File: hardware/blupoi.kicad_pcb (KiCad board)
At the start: 2 copper layers, 505.1 x 22.2 mm, 208 parts, among them P1 MICRO-B-USB, SW1 PM_BTN, U1 NRF52832, U2 TPS63031DSKR, U3 bno055, U4 ics43432, U5 BQ24075RGTT, U6 MAX16054AZT+T, X1 32MHz

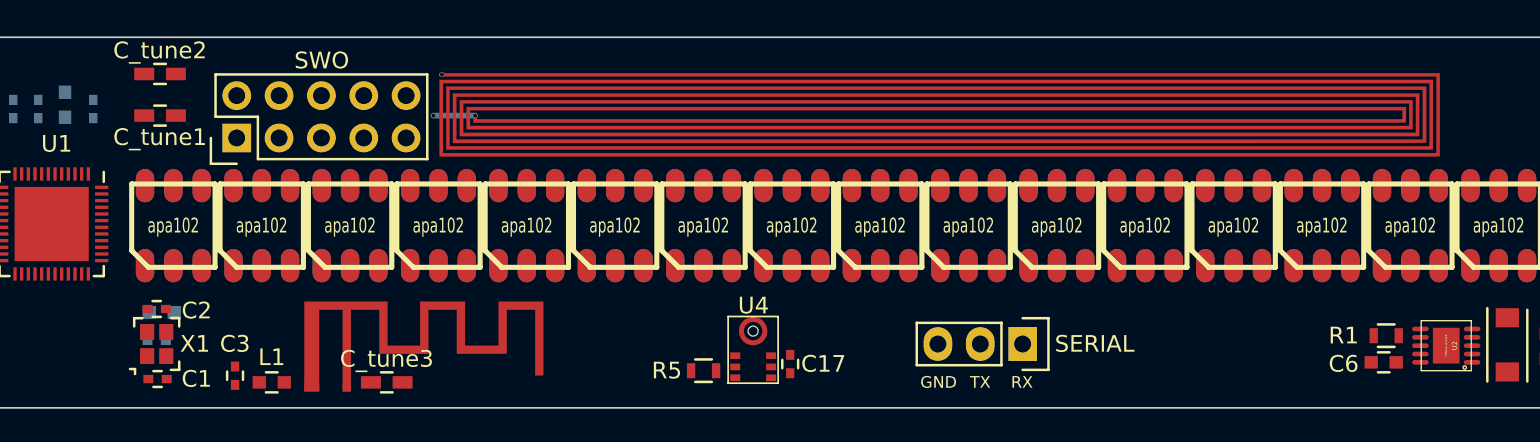
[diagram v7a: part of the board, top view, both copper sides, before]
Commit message: Increased MIC pad sizes
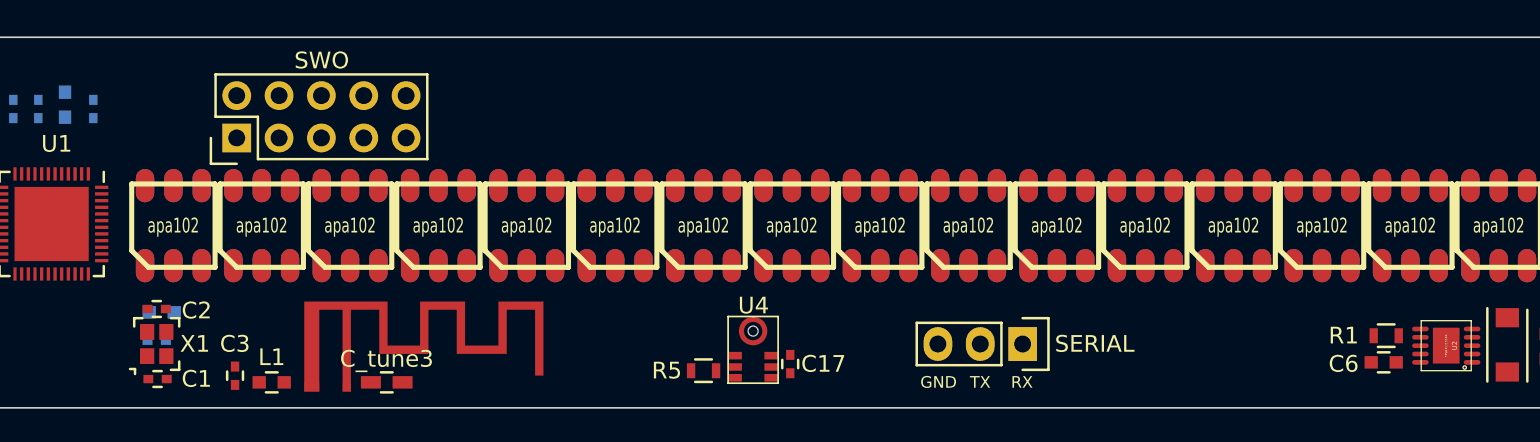
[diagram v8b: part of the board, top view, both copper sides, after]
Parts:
- removed ANT2: ANT_NFC, nfc_antenna:nfc_antenna_60x5mm_1.826uH
- removed C_tune1, C_tune2: TDB, Capacitors_SMD:C_0603_HandSoldering
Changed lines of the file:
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@@
 (kicad_pcb (version 20170123) (host pcbnew no-vcs-found-7591~57~ubuntu16.10.1)
   (general
-    (links 799)
-    (no_connects 783)
+    (links 793)
+    (no_connects 777)
     (area -67.365001 99.149999 437.850001 121.480001)
     (thickness 1.6)
@@
     (tracks 0)
     (zones 0)
-    (modules 208)
+    (modules 205)
     (nets 345)
   )
@@
     (pad 4 smd circle (at 1.1565 1.5 90) (size 1.65 1.65) (layers F.Paste F.Mask)
       (net 2 GND))
-    (pad 7 smd rect (at -1.6435 0.425 90) (size 0.4 0.6) (layers F.Cu F.Paste F.Mask)
+    (pad 7 smd rect (at -1.6435 0.425 90) (size 0.45 0.8) (layers F.Cu F.Paste F.Mask)
       (net 322 MIC_I2S_SD))
-    (pad 6 smd rect (at -0.9935 0.425 90) (size 0.4 0.6) (layers F.Cu F.Paste F.Mask)
+    (pad 6 smd rect (at -0.9935 0.425 90) (size 0.45 0.8) (layers F.Cu F.Paste F.Mask)
       (net 324 MIC_I2S_SCK))
-    (pad 5 smd rect (at -0.3185 0.425 90) (size 0.4 0.6) (layers F.Cu F.Paste F.Mask)
+    (pad 5 smd rect (at -0.3185 0.425 90) (size 0.45 0.8) (layers F.Cu F.Paste F.Mask)
       (net 325 MIC_I2S_WS))
-    (pad 3 smd rect (at -0.3185 2.575 90) (size 0.4 0.6) (layers F.Cu F.Paste F.Mask)
+    (pad 3 smd rect (at -0.3185 2.575 90) (size 0.45 0.8) (layers F.Cu F.Paste F.Mask)
       (net 328 V3.3))
-    (pad 2 smd rect (at -0.9935 2.575 90) (size 0.4 0.6) (layers F.Cu F.Paste F.Mask)
+    (pad 2 smd rect (at -0.9935 2.575 90) (size 0.45 0.8) (layers F.Cu F.Paste F.Mask)
       (net 2 GND))
-    (pad 1 smd rect (at -1.6435 2.575 90) (size 0.4 0.6) (layers F.Cu F.Paste F.Mask)
+    (pad 1 smd rect (at -1.6435 2.575 90) (size 0.45 0.8) (layers F.Cu F.Paste F.Mask)
       (net 328 V3.3))
   )
@@
   )
   (module Capacitors_SMD:C_0603_HandSoldering (layer F.Cu)
-    (at -44.5 103.9)
-    (descr "Capacitor SMD 0603, hand soldering")
-    (tags "capacitor 0603")
-    (attr smd)
-    (fp_text reference C_tune1 (at 0 1.3 -180) (layer F.SilkS)
-      (effects (font (size 1 1) (thickness 0.15)))
-    )
-    (fp_text value TDB (at 0 1.9) (layer F.Fab)
-      (effects (font (size 1 1) (thickness 0.15)))
-    )
-    (fp_line (start -1.85 -0.75) (end 1.85 -0.75) (layer F.CrtYd) (width 0.05))
-    (fp_line (start -1.85 0.75) (end 1.85 0.75) (layer F.CrtYd) (width 0.05))
-    (fp_line (start -1.85 -0.75) (end -1.85 0.75) (layer F.CrtYd) (width 0.05))
-    (fp_line (start 1.85 -0.75) (end 1.85 0.75) (layer F.CrtYd) (width 0.05))
-    (fp_line (start -0.35 -0.6) (end 0.35 -0.6) (layer F.SilkS) (width 0.15))
-    (fp_line (start 0.35 0.6) (end -0.35 0.6) (layer F.SilkS) (width 0.15))
-    (pad 1 smd rect (at -0.95 0) (size 1.2 0.75) (layers F.Cu F.Paste F.Mask)
-      (net 2 GND))
-    (pad 2 smd rect (at 0.95 0) (size 1.2 0.75) (layers F.Cu F.Paste F.Mask)
-      (net 133 "Net-(ANT2-Pad1)"))
-    (model Capacitors_SMD.3dshapes/C_0603_HandSoldering.wrl
-      (at (xyz 0 0 0))
-      (scale (xyz 1 1 1))
-      (rotate (xyz 0 0 0))
-    )
-  )
-  (module Capacitors_SMD:C_0603_HandSoldering (layer F.Cu)
-    (at -44.5 101.4 180)
-    (descr "Capacitor SMD 0603, hand soldering")
-    (tags "capacitor 0603")
-    (attr smd)
-    (fp_text reference C_tune2 (at 0 1.4) (layer F.SilkS)
-      (effects (font (size 1 1) (thickness 0.15)))
-    )
-    (fp_text value TDB (at 0 1.9 180) (layer F.Fab)
-      (effects (font (size 1 1) (thickness 0.15)))
-    )
-    (fp_line (start -1.85 -0.75) (end 1.85 -0.75) (layer F.CrtYd) (width 0.05))
-    (fp_line (start -1.85 0.75) (end 1.85 0.75) (layer F.CrtYd) (width 0.05))
-    (fp_line (start -1.85 -0.75) (end -1.85 0.75) (layer F.CrtYd) (width 0.05))
-    (fp_line (start 1.85 -0.75) (end 1.85 0.75) (layer F.CrtYd) (width 0.05))
-    (fp_line (start -0.35 -0.6) (end 0.35 -0.6) (layer F.SilkS) (width 0.15))
-    (fp_line (start 0.35 0.6) (end -0.35 0.6) (layer F.SilkS) (width 0.15))
-    (pad 1 smd rect (at -0.95 0 180) (size 1.2 0.75) (layers F.Cu F.Paste F.Mask)
-      (net 139 "Net-(ANT2-Pad2)"))
-    (pad 2 smd rect (at 0.95 0 180) (size 1.2 0.75) (layers F.Cu F.Paste F.Mask)
-      (net 2 GND))
-    (model Capacitors_SMD.3dshapes/C_0603_HandSoldering.wrl
-      (at (xyz 0 0 0))
-      (scale (xyz 1 1 1))
-      (rotate (xyz 0 0 0))
-    )
-  )
-  (module Capacitors_SMD:C_0603_HandSoldering (layer F.Cu)
     (at -30.9 119.9)
     (descr "Capacitor SMD 0603, hand soldering")
@@
     )
   )
-  (module nfc_antenna:nfc_antenna_60x5mm_1.826uH (layer F.Cu)
-    (at 2.255 103.85)
-    (fp_text reference ANT2 (at 0.0635 -5.08) (layer F.SilkS) hide
-      (effects (font (thickness 0.3)))
-    )
-    (fp_text value ANT_NFC (at 0 -3.429) (layer F.SilkS) hide
-      (effects (font (thickness 0.3)))
-    )
-    (fp_line (start -27.8765 0.05) (end -30.353 0.05) (layer B.Cu) (width 0.35))
-    (fp_poly (pts (xy 30.011709 0.002646) (xy 30.009042 2.502958) (xy 0.007937 2.505606) (xy -29.993167 2.508254)
-      (xy -29.993167 -2.0955) (xy 29.601636 -2.0955) (xy 29.596292 2.090208) (xy -29.591 2.095504)
-      (xy -29.591 -1.693333) (xy 29.199417 -1.693333) (xy 29.199416 -0.015119) (xy 29.199396 0.208707)
-      (xy 29.19933 0.412297) (xy 29.199209 0.596581) (xy 29.199026 0.762489) (xy 29.198771 0.910953)
-      (xy 29.198437 1.042903) (xy 29.198016 1.159269) (xy 29.197498 1.260981) (xy 29.196877 1.34897)
-      (xy 29.196142 1.424167) (xy 29.195287 1.487501) (xy 29.194303 1.539904) (xy 29.193181 1.582306)
-      (xy 29.191914 1.615637) (xy 29.190492 1.640827) (xy 29.188908 1.658808) (xy 29.187153 1.670509)
-      (xy 29.18522 1.676861) (xy 29.184297 1.678214) (xy 29.181827 1.678713) (xy 29.175277 1.679202)
-      (xy 29.164426 1.67968) (xy 29.14905 1.680147) (xy 29.128928 1.680603) (xy 29.103837 1.68105)
-      (xy 29.073554 1.681486) (xy 29.037858 1.681911) (xy 28.996525 1.682327) (xy 28.949333 1.682733)
-      (xy 28.896061 1.683129) (xy 28.836485 1.683515) (xy 28.770383 1.683892) (xy 28.697533 1.684259)
-      (xy 28.617712 1.684617) (xy 28.530697 1.684966) (xy 28.436268 1.685305) (xy 28.3342 1.685636)
-      (xy 28.224272 1.685957) (xy 28.106261 1.68627) (xy 27.979945 1.686574) (xy 27.845101 1.68687)
-      (xy 27.701507 1.687157) (xy 27.548941 1.687436) (xy 27.38718 1.687707) (xy 27.216001 1.687969)
-      (xy 27.035183 1.688224) (xy 26.844503 1.688471) (xy 26.643738 1.68871) (xy 26.432667 1.688941)
-      (xy 26.211066 1.689165) (xy 25.978713 1.689381) (xy 25.735386 1.68959) (xy 25.480862 1.689792)
-      (xy 25.214919 1.689987) (xy 24.937335 1.690175) (xy 24.647887 1.690357) (xy 24.346353 1.690531)
-      (xy 24.03251 1.690699) (xy 23.706136 1.69086) (xy 23.367009 1.691015) (xy 23.014906 1.691164)
-      (xy 22.649604 1.691307) (xy 22.270881 1.691444) (xy 21.878516 1.691574) (xy 21.472285 1.691699)
-      (xy 21.051966 1.691819) (xy 20.617336 1.691932) (xy 20.168174 1.692041) (xy 19.704256 1.692144)
-      (xy 19.225361 1.692241) (xy 18.731266 1.692334) (xy 18.221748 1.692422) (xy 17.696585 1.692505)
-      (xy 17.155556 1.692583) (xy 16.598436 1.692656) (xy 16.025004 1.692725) (xy 15.435038 1.69279)
-      (xy 14.828315 1.69285) (xy 14.204612 1.692906) (xy 13.563708 1.692958) (xy 12.905379 1.693006)
-      (xy 12.229404 1.69305) (xy 11.53556 1.693091) (xy 10.823624 1.693128) (xy 10.093375 1.693161)
-      (xy 9.344589 1.693191) (xy 8.577045 1.693218) (xy 7.79052 1.693242) (xy 6.984791 1.693263)
-      (xy 6.159636 1.69328) (xy 5.314832 1.693295) (xy 4.450159 1.693308) (xy 3.565391 1.693317)
-      (xy 2.660309 1.693325) (xy 1.734688 1.69333) (xy 0.788307 1.693332) (xy -0.009828 1.693333)
-      (xy -29.188833 1.693333) (xy -29.188833 -1.280583) (xy 28.786751 -1.280583) (xy 28.781375 1.285875)
-      (xy 0.002646 1.288523) (xy -28.776083 1.29117) (xy -28.776083 -0.878417) (xy 28.384622 -0.878417)
-      (xy 28.379208 0.873125) (xy 0.002646 0.875773) (xy -28.373917 0.87842) (xy -28.373917 -0.465667)
-      (xy 27.982553 -0.465667) (xy 27.979797 0.002646) (xy 27.977042 0.470958) (xy 0.007937 0.473606)
-      (xy -27.961167 0.476254) (xy -27.961167 -0.0635) (xy -27.7495 -0.0635) (xy -27.7495 0.264583)
-      (xy 27.770667 0.264583) (xy 27.770667 -0.264583) (xy -28.16225 -0.264583) (xy -28.16225 0.66675)
-      (xy 28.172833 0.66675) (xy 28.172833 -0.677333) (xy -28.564417 -0.677333) (xy -28.564417 1.0795)
-      (xy 28.575 1.0795) (xy 28.575 -1.0795) (xy -28.977167 -1.0795) (xy -28.977167 1.481667)
-      (xy 28.98775 1.481667) (xy 28.98775 -1.49225) (xy -29.379333 -1.49225) (xy -29.379333 1.883833)
-      (xy 29.389917 1.883833) (xy 29.389917 -1.894417) (xy -29.7815 -1.894417) (xy -29.7815 2.296583)
-      (xy 29.802667 2.296583) (xy 29.802667 -2.296583) (xy -29.993167 -2.296583) (xy -29.993167 -2.497667)
-      (xy 30.014377 -2.497667) (xy 30.011709 0.002646)) (layer F.Cu) (width 0.01))
-    (pad "" thru_hole circle (at -27.855 0.05) (size 0.3 0.3) (drill 0.25) (layers *.Cu *.Mask F.SilkS))
-    (pad 2 thru_hole circle (at -29.845 -2.413) (size 0.3 0.3) (drill 0.25) (layers *.Cu *.Mask F.SilkS)
-      (net 139 "Net-(ANT2-Pad2)"))
-    (pad 1 thru_hole circle (at -30.353 0.05) (size 0.3 0.3) (drill 0.25) (layers *.Cu *.Mask F.SilkS)
-      (net 133 "Net-(ANT2-Pad1)"))
-  )
   (module bno055:bno055 (layer F.Cu)
